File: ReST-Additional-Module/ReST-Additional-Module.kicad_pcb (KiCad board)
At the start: 2 copper layers, 19.2 x 38.8 mm, 11 parts, among them P1 CONN_02X06, P2 02-SCREW-TERM, P3 02-SCREW-TERM, Q1 Q_BSH105, Q2 Q_AOT240L

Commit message: Fixed GND Connection on ADD Board
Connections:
- P1 pad 2: GND -> (no net)
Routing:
- net GND: track 0.00 -> 17.7 mm, vias 0 -> 1
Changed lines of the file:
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@@
 (kicad_pcb (version 4) (host pcbnew 4.0.1-stable)
   (general
-    (links 25)
-    (no_connects 2)
-    (area 0 0 0 0)
+    (links 24)
+    (no_connects 0)
+    (area 88.549999 86.149999 107.850001 125.050001)
     (thickness 1.6)
-    (drawings 7)
-    (tracks 65)
+    (drawings 8)
+    (tracks 73)
     (zones 0)
     (modules 11)
@@
     (pad 1 thru_hole rect (at 0 0 270) (size 1.7272 1.7272) (drill 1.016) (layers *.Cu *.Mask F.SilkS)
       (net 6 +5V))
-    (pad 2 thru_hole oval (at 2.54 0 270) (size 1.7272 1.7272) (drill 1.016) (layers *.Cu *.Mask F.SilkS)
-      (net 5 GND))
+    (pad 2 thru_hole oval (at 2.54 0 270) (size 1.7272 1.7272) (drill 1.016) (layers *.Cu *.Mask F.SilkS))
     (pad 3 thru_hole oval (at 0 2.54 270) (size 1.7272 1.7272) (drill 1.016) (layers *.Cu *.Mask F.SilkS)
       (net 8 /PWM-ADD))
@@
       (net 6 +5V))
   )
+  (target plus (at 88.6 125) (size 5) (width 0.1) (layer Edge.Cuts))
   (gr_line (start 88.6 125) (end 89.4 125) (angle 90) (layer Edge.Cuts) (width 0.1))
   (gr_line (start 88.6 107.6) (end 88.6 125) (angle 90) (layer Edge.Cuts) (width 0.1))
@@
   (segment (start 99.19992 101) (end 99.19992 97.20008) (width 2) (layer F.Cu) (net 4))
   (segment (start 99.19992 97.20008) (end 99.4 97) (width 2) (layer F.Cu) (net 4))
+  (segment (start 102.50076 115.45) (end 102.50076 114.70076) (width 0.25) (layer F.Cu) (net 5))
+  (segment (start 92 119.3) (end 93 120.3) (width 0.25) (layer B.Cu) (net 5))
+  (segment (start 92 115) (end 92 119.3) (width 0.25) (layer B.Cu) (net 5))
+  (segment (start 92.8 114.2) (end 92 115) (width 0.25) (layer B.Cu) (net 5))
+  (segment (start 101.6 114.2) (end 92.8 114.2) (width 0.25) (layer B.Cu) (net 5))
+  (segment (start 101.8 114) (end 101.6 114.2) (width 0.25) (layer B.Cu) (net 5))
+  (via (at 101.8 114) (size 0.6) (drill 0.4) (layers F.Cu B.Cu) (net 5))
+  (segment (start 102.50076 114.70076) (end 101.8 114) (width 0.25) (layer F.Cu) (net 5))
   (segment (start 94.8 117.87546) (end 93.77546 117.87546) (width 0.25) (layer F.Cu) (net 6))
   (segment (start 104.8 116.9) (end 105.7 116) (width 0.25) (layer F.Cu) (net 6))

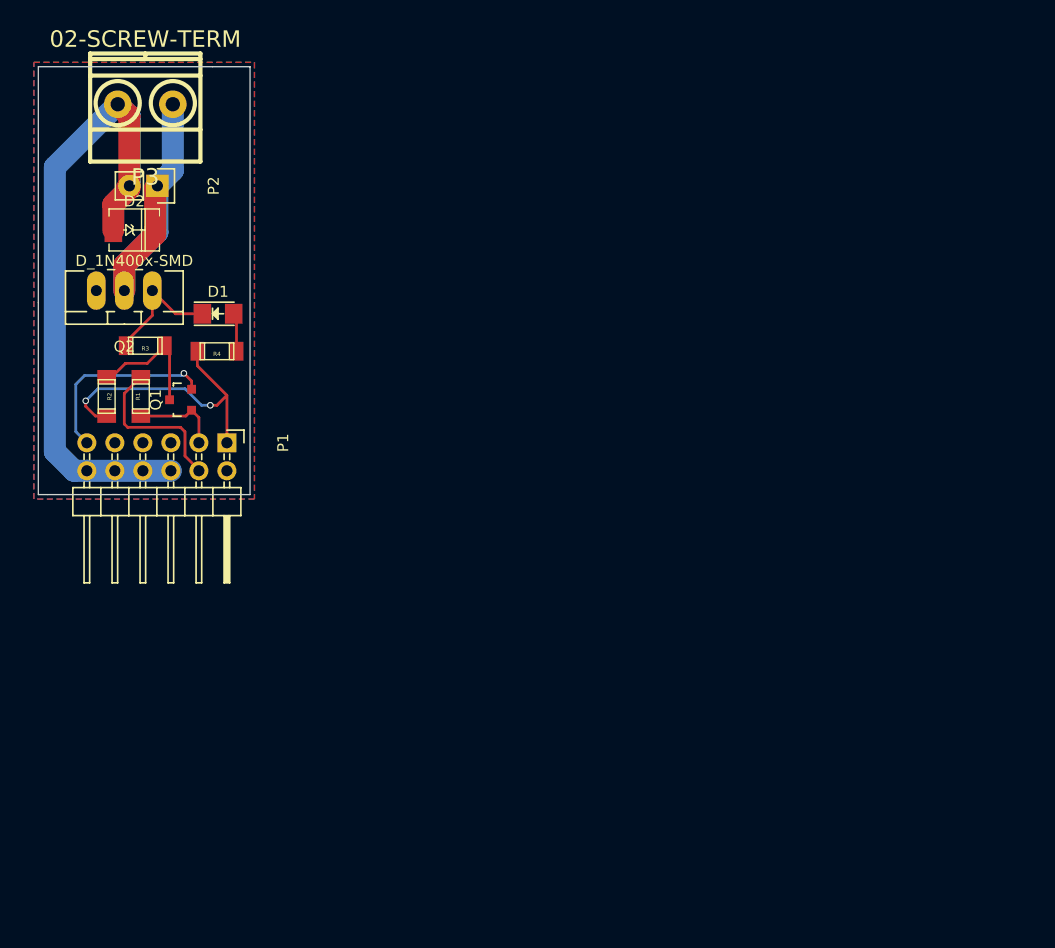
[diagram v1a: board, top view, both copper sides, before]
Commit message: Changed Additional-Board and Pinout
Sooo... I thought adding multiple Additional Module Boards would be bit much. Looked back at some older projects of mine and thought that using something like the uln2803 would be pretty neat (like 8 NPN Transitors, each 500mah and that in a DIL-18 Package IIRC) Which turns price really down, aswell as the size of the module. 
But using that one resultet in removing many extra pinouts, leaving with only 5 unused pins which will be broken out extra. This may change when the lcd pinout is finished. adding extra pinout for the additional board could also work out (as it occupies 8 pwm pins). I will look to copy that all into the schematic

Also missing: I2C EEPROM/Flash for settings
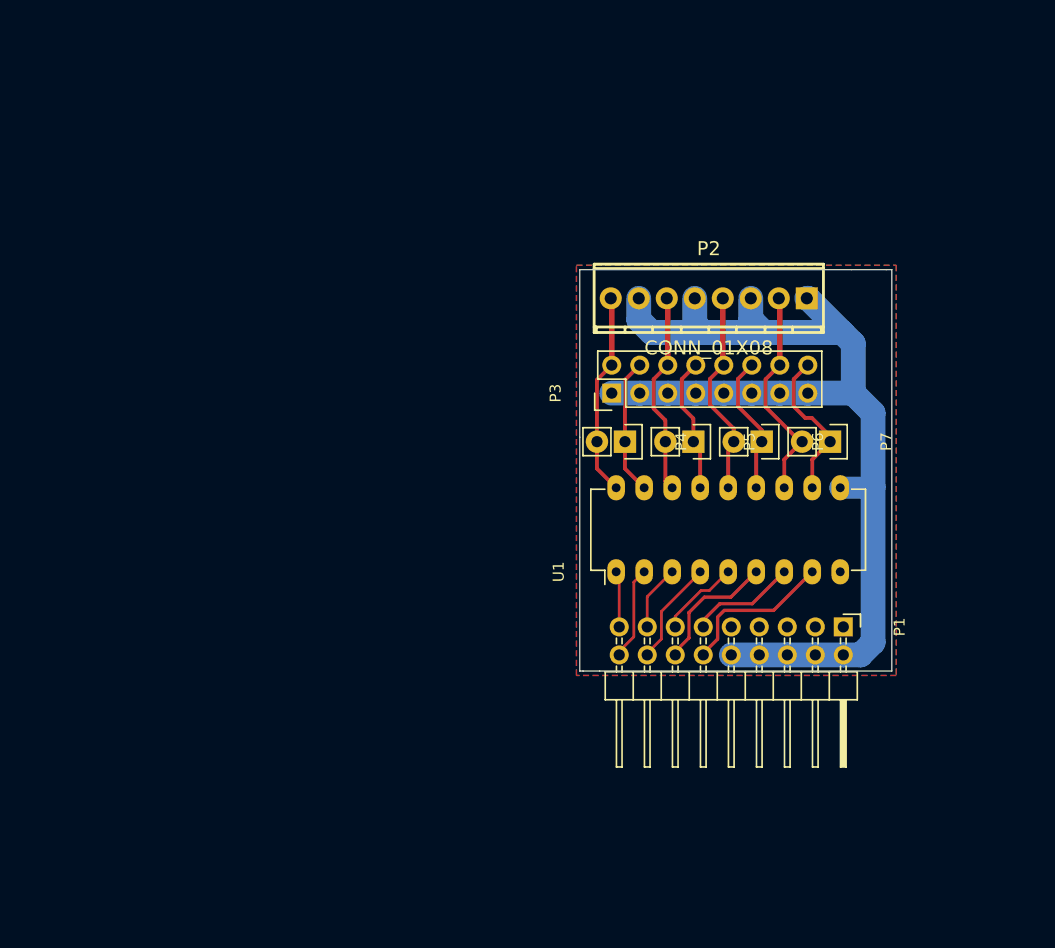
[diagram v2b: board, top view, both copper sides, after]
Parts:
- removed D1: LED, LEDs:LED_1206
- removed D2: D_1N400x-SMD, DO-214AC(SMA):DO-214AC(SMA)
- removed Q1: Q_BSH105, TO_SOT_Packages_SMD:SOT-23
- removed Q2: Q_AOT240L, TO_SOT_Packages_THT:TO-220_Neutral123_Vertical_LargePads
- removed R1, R2: 100K, ok-smd-generic:1206
- removed R3: 22R, ok-smd-generic:1206
- removed R4: 470R, ok-smd-generic:1206
- added P4: CONN_01X02, Pin_Headers:Pin_Header_Straight_1x02, F.Cu at (141.8, 120.2)
- added P5: CONN_01X02, Pin_Headers:Pin_Header_Straight_1x02, F.Cu at (148.0, 120.2)
- added P6: CONN_01X02, Pin_Headers:Pin_Header_Straight_1x02, F.Cu at (154.2, 120.2)
- added P7: CONN_01X02, Pin_Headers:Pin_Header_Straight_1x02, F.Cu at (160.4, 120.2)
- added U1: ULN2803, Housings_DIP:DIP-18_W7.62mm_LongPads, F.Cu at (141.0, 132.0)
- P1: value CONN_02X06 -> CONN_02X09; footprint Pin_Headers:Pin_Header_Angled_2x06 -> Pin_Headers:Pin_Header_Angled_2x09
- P2: value 02-SCREW-TERM -> CONN_01X08; footprint Pin_Headers:Pin_Header_Straight_1x02 -> 2:mpt_0,5%2f8-2,54
- P3: value 02-SCREW-TERM -> CONN_02X08; footprint 5mm-pitch-terminal:mkds_1,5-2 -> Pin_Headers:Pin_Header_Straight_2x08
- moved P1 58.3 mm to (161.6, 137.0)
- moved P2 51.0 mm to (149.4, 107.2), turned to 0 degrees
- moved P3 49.8 mm to (140.6, 115.8), turned to 90 degrees
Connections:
- P1 pad 1: +5V -> GND
- P1 pad 11: GND -> /PWM-ADD6
- P1 pad 12: +12V -> /PWM-ADD7
- P1 pad 2: (no net) -> +12V
- P1 pad 3: /PWM-ADD -> GND
- P1 pad 4: +3V3 -> +12V
- P2 pad 1: Net-(D2-Pad2) -> +12V
- P2 pad 2: +12V -> /PWM-OUT6
- P3 pad 1: Net-(D2-Pad2) -> +12V
- P3 pad 2: +12V -> /PWM-OUT0
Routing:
- net +12V: track 65.8 -> 100.1 mm
- net Net-(D2-Pad2): track 29.5 -> 0.00 mm
- net +5V: track 26.4 -> 0.00 mm, vias 2 -> 0
- net /PWM-OUT6: track 0.00 -> 19.9 mm
- net /PWM-OUT4: track 0.00 -> 18.8 mm
- net /PWM-OUT0: track 0.00 -> 18.5 mm
- net /PWM-OUT2: track 0.00 -> 18.4 mm
- net GND: track 17.7 -> 0.00 mm, vias 1 -> 0
- net +3V3: track 14.7 -> 0.00 mm
- net /PWM-ADD7: track 0.00 -> 14.3 mm
- net /PWM-OUT7: track 0.00 -> 14.0 mm
- net /PWM-OUT5: track 0.00 -> 12.7 mm
- net /PWM-OUT1: track 0.00 -> 12.4 mm
- net /PWM-OUT3: track 0.00 -> 12.3 mm
- net /PWM-ADD5: track 0.00 -> 12.0 mm
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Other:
- board size 19.2 x 38.8 mm -> 28.3 x 36.4 mm

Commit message: Changed ADD Board to use less Pins
Now only 4 Channels, but everyone ~0.6A capable
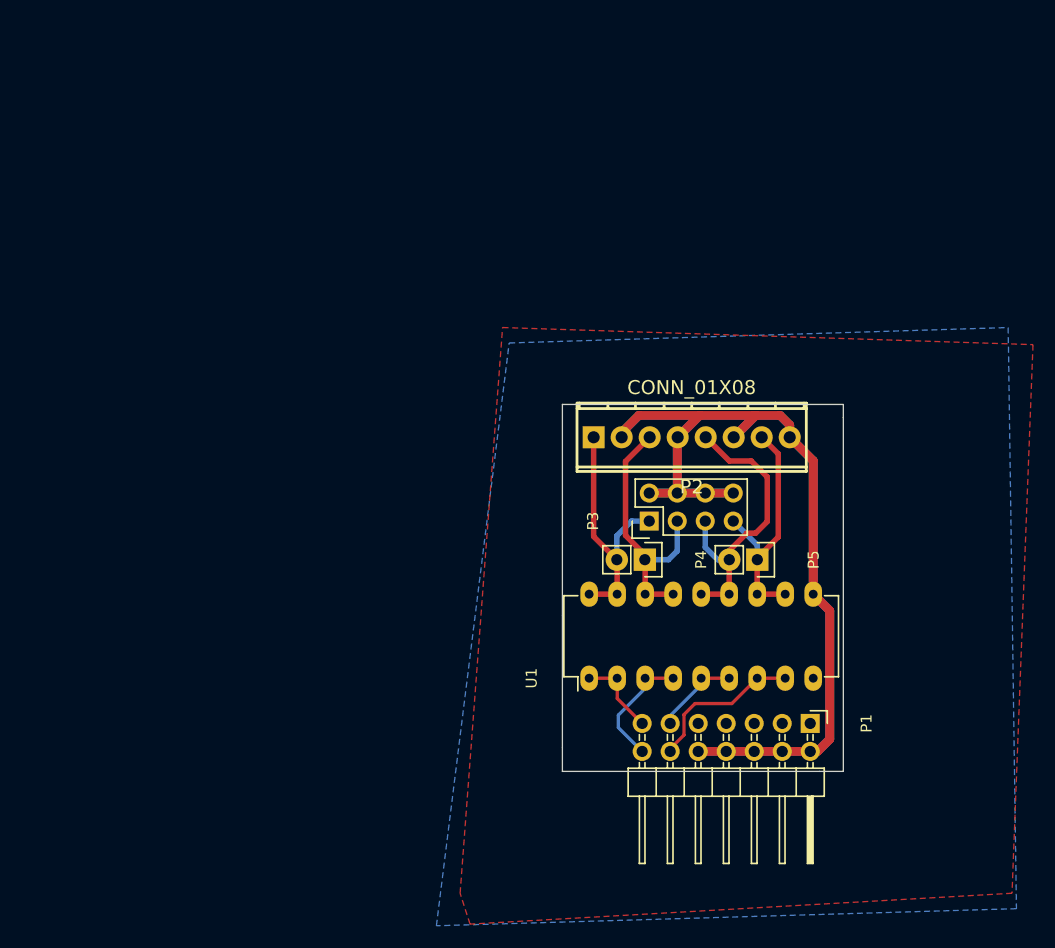
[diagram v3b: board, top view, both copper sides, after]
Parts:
- removed P6, P7: CONN_01X02, Pin_Headers:Pin_Header_Straight_1x02
- P1: value CONN_02X09 -> CONN_02X07; footprint Pin_Headers:Pin_Header_Angled_2x09 -> Pin_Headers:Pin_Header_Angled_2x07
- P3: value CONN_02X08 -> CONN_02X04; footprint Pin_Headers:Pin_Header_Straight_2x08 -> Pin_Headers:Pin_Header_Straight_2x04
- moved P2 12.7 mm to (147.8, 119.8), turned to 180 degrees
- moved P5 12.2 mm to (153.8, 130.9)
- moved P3 12.1 mm to (144.0, 127.4)
- moved P4 10.9 mm to (143.6, 130.9)
- moved U1 9.96 mm to (138.6, 141.7)
- moved P1 9.25 mm to (158.6, 145.8)
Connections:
- P1 pad 11: /PWM-ADD6 -> /PWM-ADD2
- P1 pad 12: /PWM-ADD7 -> /PWM-ADD3
- P1 pad 13: /PWM-ADD4 -> /PWM-ADD0
- P1 pad 14: /PWM-ADD5 -> /PWM-ADD1
- P2 pad 1: +12V -> /PWM-OUT0
- P2 pad 2: /PWM-OUT6 -> +12V
- P2 pad 3: +12V -> /PWM-OUT1
- P2 pad 4: /PWM-OUT4 -> +12V
- P2 pad 5: +12V -> /PWM-OUT2
- P2 pad 6: /PWM-OUT2 -> +12V
- P2 pad 7: +12V -> /PWM-OUT3
- P2 pad 8: /PWM-OUT0 -> +12V
- P3 pad 1: +12V -> /PWM-OUT0
- P3 pad 2: /PWM-OUT0 -> +12V
- P3 pad 3: +12V -> /PWM-OUT1
- P3 pad 4: /PWM-OUT1 -> +12V
- P3 pad 5: +12V -> /PWM-OUT2
- P3 pad 6: /PWM-OUT2 -> +12V
- P3 pad 7: +12V -> /PWM-OUT3
- P3 pad 8: /PWM-OUT3 -> +12V
- U1 pad 11: /PWM-OUT7 -> /PWM-OUT3
- U1 pad 12: /PWM-OUT6 -> /PWM-OUT3
- U1 pad 13: /PWM-OUT5 -> /PWM-OUT2
- U1 pad 14: /PWM-OUT4 -> /PWM-OUT2
- U1 pad 15: /PWM-OUT3 -> /PWM-OUT1
- U1 pad 16: /PWM-OUT2 -> /PWM-OUT1
- U1 pad 17: /PWM-OUT1 -> /PWM-OUT0
- U1 pad 2: /PWM-ADD1 -> /PWM-ADD0
- U1 pad 3: /PWM-ADD2 -> /PWM-ADD1
- U1 pad 4: /PWM-ADD3 -> /PWM-ADD1
- U1 pad 5: /PWM-ADD4 -> /PWM-ADD2
- U1 pad 6: /PWM-ADD5 -> /PWM-ADD2
- U1 pad 7: /PWM-ADD6 -> /PWM-ADD3
- U1 pad 8: /PWM-ADD7 -> /PWM-ADD3
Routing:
- net +12V: track 100.1 -> 154.9 mm
- net /PWM-OUT6: track 19.9 -> 0.00 mm
- net /PWM-OUT4: track 18.8 -> 0.00 mm
- net /PWM-ADD7: track 14.3 -> 0.00 mm
- net /PWM-OUT7: track 14.0 -> 0.00 mm
- net /PWM-OUT5: track 12.7 -> 0.00 mm
- net /PWM-OUT1: track 12.4 -> 24.4 mm
- net /PWM-ADD5: track 12.0 -> 0.00 mm
- net /PWM-OUT3: track 12.3 -> 22.6 mm
- net /PWM-ADD6: track 9.76 -> 0.00 mm
- net /PWM-OUT2: track 18.4 -> 27.2 mm
- net /PWM-ADD4: track 7.43 -> 0.00 mm
- net /PWM-ADD3: track 9.53 -> 14.4 mm
- net /PWM-OUT0: track 18.5 -> 23.3 mm
- net /PWM-ADD1: track 8.48 -> 11.1 mm
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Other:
- board size 28.3 x 36.4 mm -> 25.5 x 33.3 mm

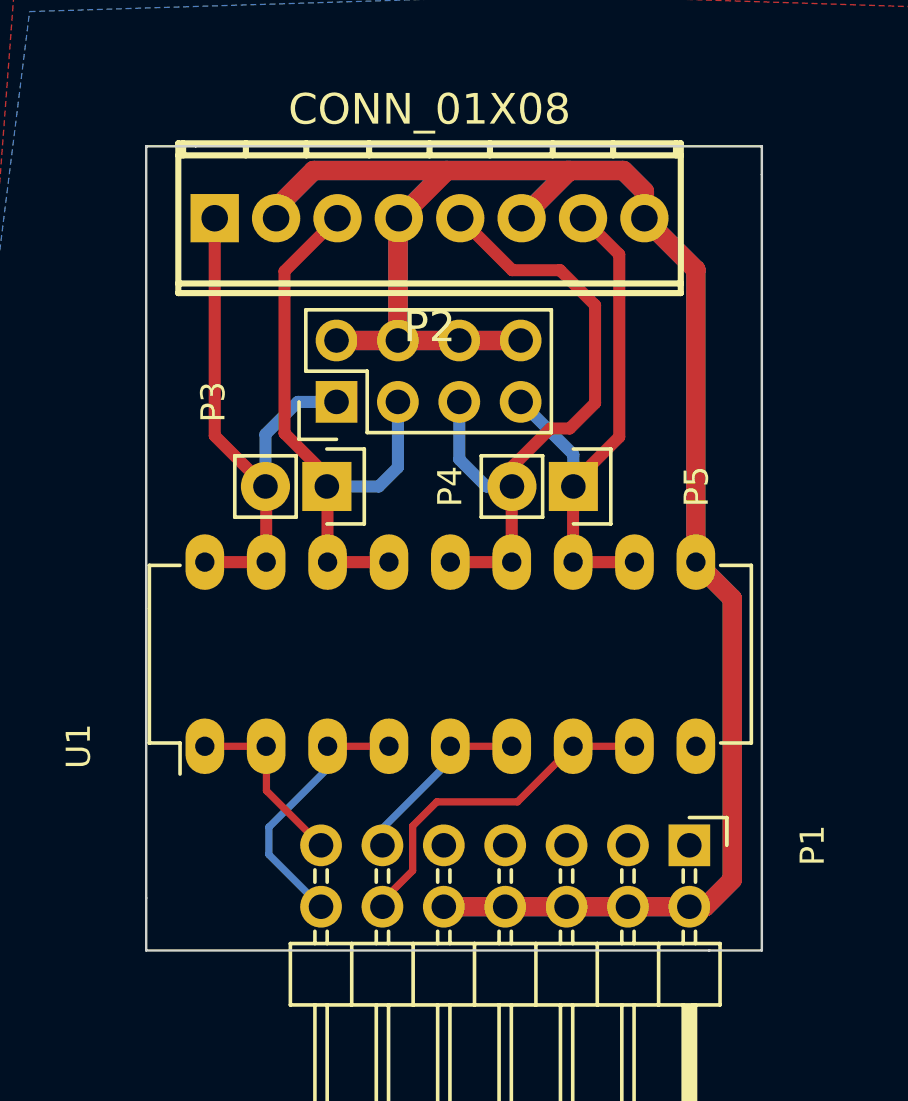
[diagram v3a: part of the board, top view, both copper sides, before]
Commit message: PRE-RELEASE Rev. A!
Yay. I managed to finish the Main PCB over the night, must say, Im happy with it. Things that changed since the last release:

Heater:
-Heater Module uses less Pins
- Much smaller Design now

Heatbed & Additional Module: 
-Changed distance from Edge to first Pin from 2.5mm to 2mm (will be changed on other boards too)

Mainboard:
-Added I2C Pullups 4K7
-Swapped Pins from Stepper, Heaters and Endstops around for easier PCB Design.
-Finished Design (10cm x 10cm!)

Added some 3D Models for testing. If someone has problems with loading some modules, please contact me! (or make a pull request with a better solution)
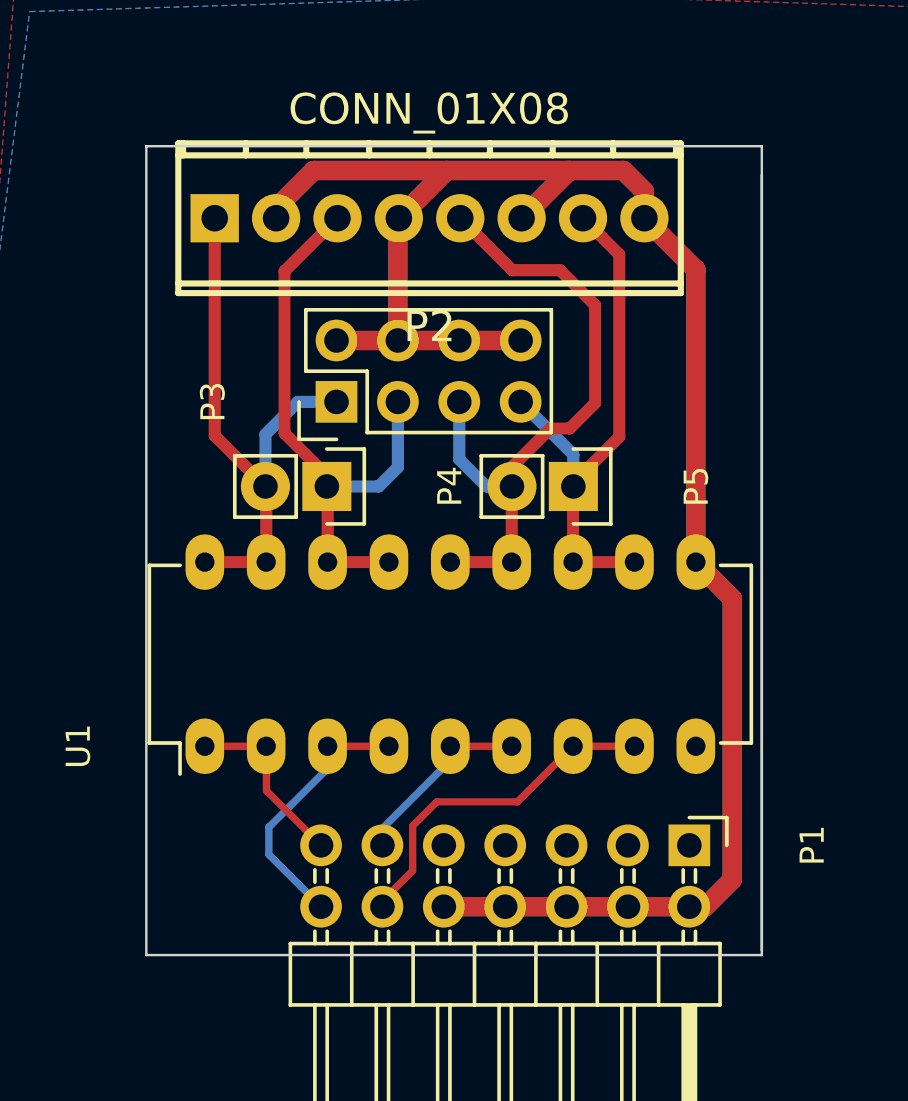
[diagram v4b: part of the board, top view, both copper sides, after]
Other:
- board size 25.5 x 33.3 mm -> 25.5 x 33.5 mm
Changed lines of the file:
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@@
     (links 42)
     (no_connects 0)
-    (area 0 0 0 0)
+    (area 124.7 109.85 178.800001 164.100001)
     (thickness 1.6)
-    (drawings 10)
+    (drawings 5)
     (tracks 114)
     (zones 0)
@@
   )
   (setup
-    (last_trace_width 0.8)
+    (last_trace_width 0.25)
     (user_trace_width 0.3)
     (user_trace_width 0.5)
@@
     )
   )
-  (gr_line (start 136.125 116.825) (end 136.125 135.95) (angle 90) (layer Edge.Cuts) (width 0.1))
-  (gr_line (start 136.15 116.825) (end 136.125 116.825) (angle 90) (layer Edge.Cuts) (width 0.1))
-  (gr_line (start 138.175 116.825) (end 136.15 116.825) (angle 90) (layer Edge.Cuts) (width 0.1))
-  (gr_line (start 161.6 116.825) (end 138.175 116.825) (angle 90) (layer Edge.Cuts) (width 0.1))
-  (gr_line (start 161.6 118) (end 161.6 116.825) (angle 90) (layer Edge.Cuts) (width 0.1))
+  (gr_line (start 161.6 150.29) (end 136.13 150.29) (angle 90) (layer Edge.Cuts) (width 0.1))
+  (gr_line (start 161.6 116.82) (end 161.6 150.29) (angle 90) (layer Edge.Cuts) (width 0.1))
+  (gr_line (start 136.13 116.82) (end 136.13 150.29) (angle 90) (layer Edge.Cuts) (width 0.1))
+  (gr_line (start 161.6 116.82) (end 136.13 116.82) (angle 90) (layer Edge.Cuts) (width 0.1))
   (gr_line (start 161.6 150.1) (end 161.6 118) (angle 90) (layer Edge.Cuts) (width 0.1))
-  (gr_line (start 159.425 150.1) (end 161.6 150.1) (angle 90) (layer Edge.Cuts) (width 0.1))
-  (gr_line (start 136.125 150.1) (end 159.425 150.1) (angle 90) (layer Edge.Cuts) (width 0.1))
-  (gr_line (start 136.125 147.925) (end 136.125 150.1) (angle 90) (layer Edge.Cuts) (width 0.1))
-  (gr_line (start 136.125 135.95) (end 136.125 147.925) (angle 90) (layer Edge.Cuts) (width 0.1))
   (segment (start 149.08 124.86) (end 151.62 124.86) (width 0.8) (layer B.Cu) (net 2))
   (segment (start 146.54 124.86) (end 149.08 124.86) (width 0.8) (layer B.Cu) (net 2))
